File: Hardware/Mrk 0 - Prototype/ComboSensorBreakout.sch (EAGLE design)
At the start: 13 parts, among them J1 CONN_42.54_SCREW, Q1 DMG3404, U1 SPG30, U2 SHTC3DFN, U3 TPS7A0518DBV, U4 TXS0102DCU

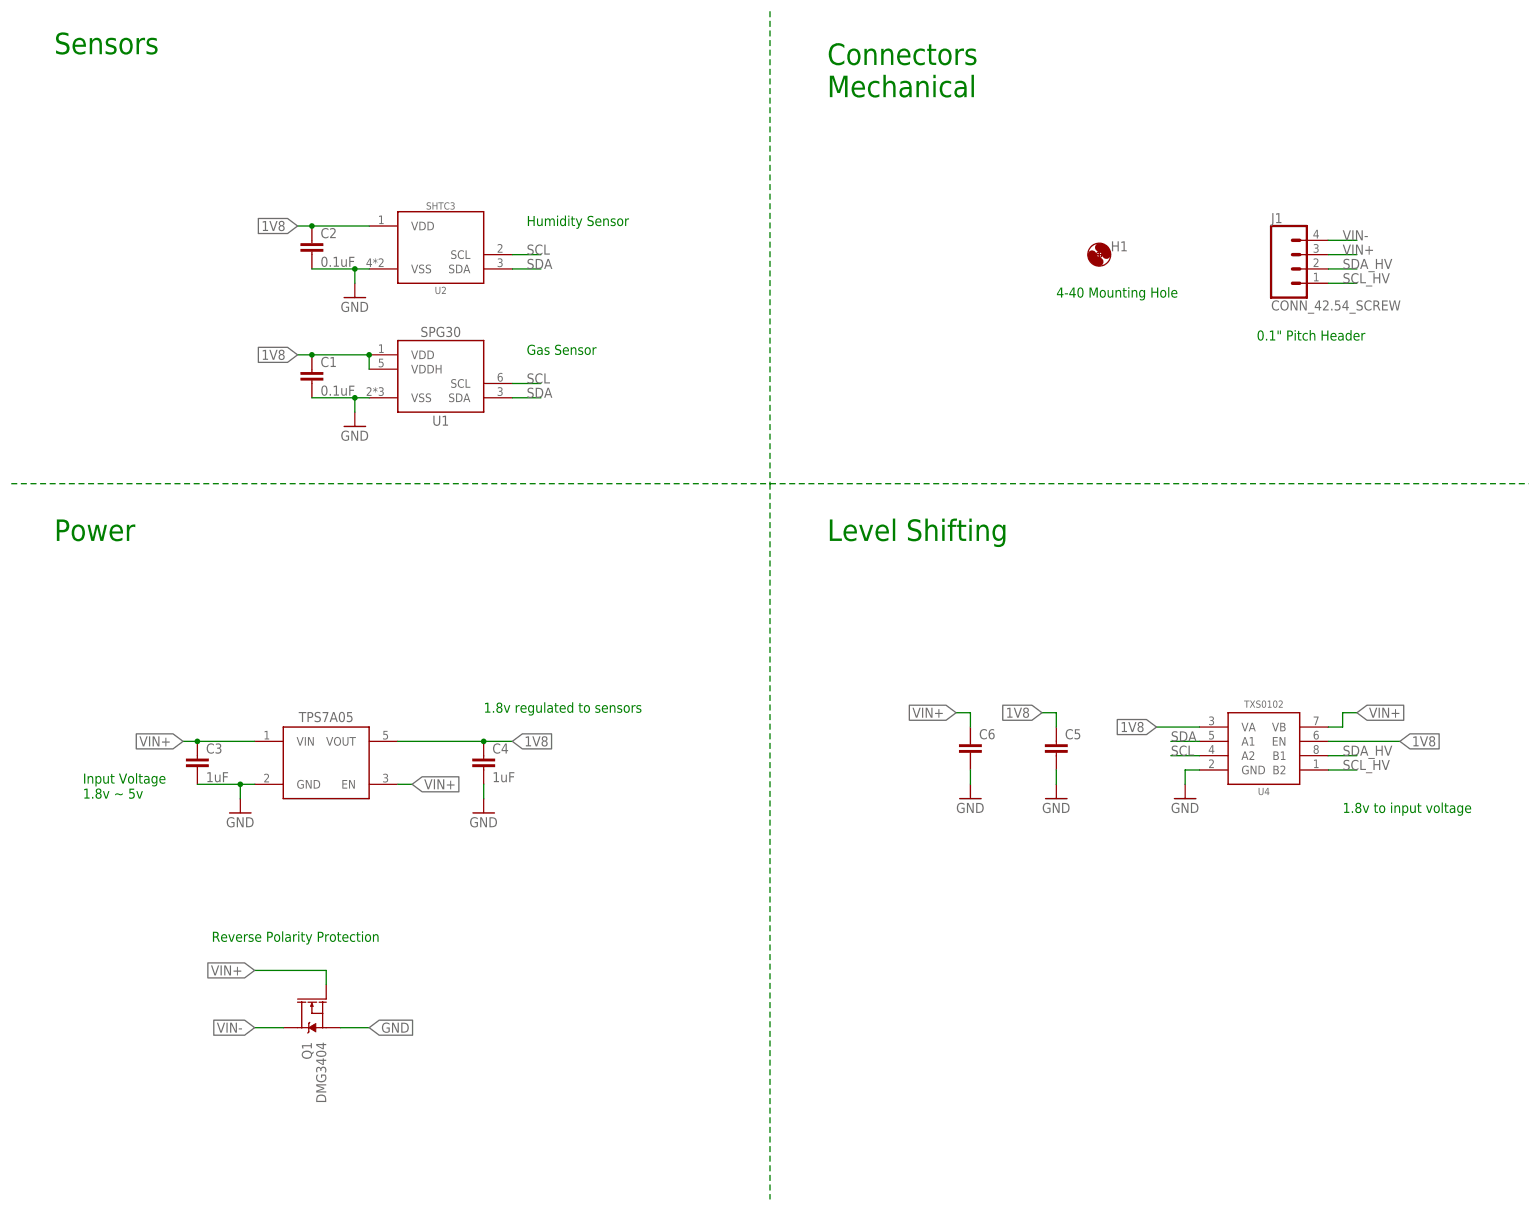
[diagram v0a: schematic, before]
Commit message: Updated/generated BoMs if not present
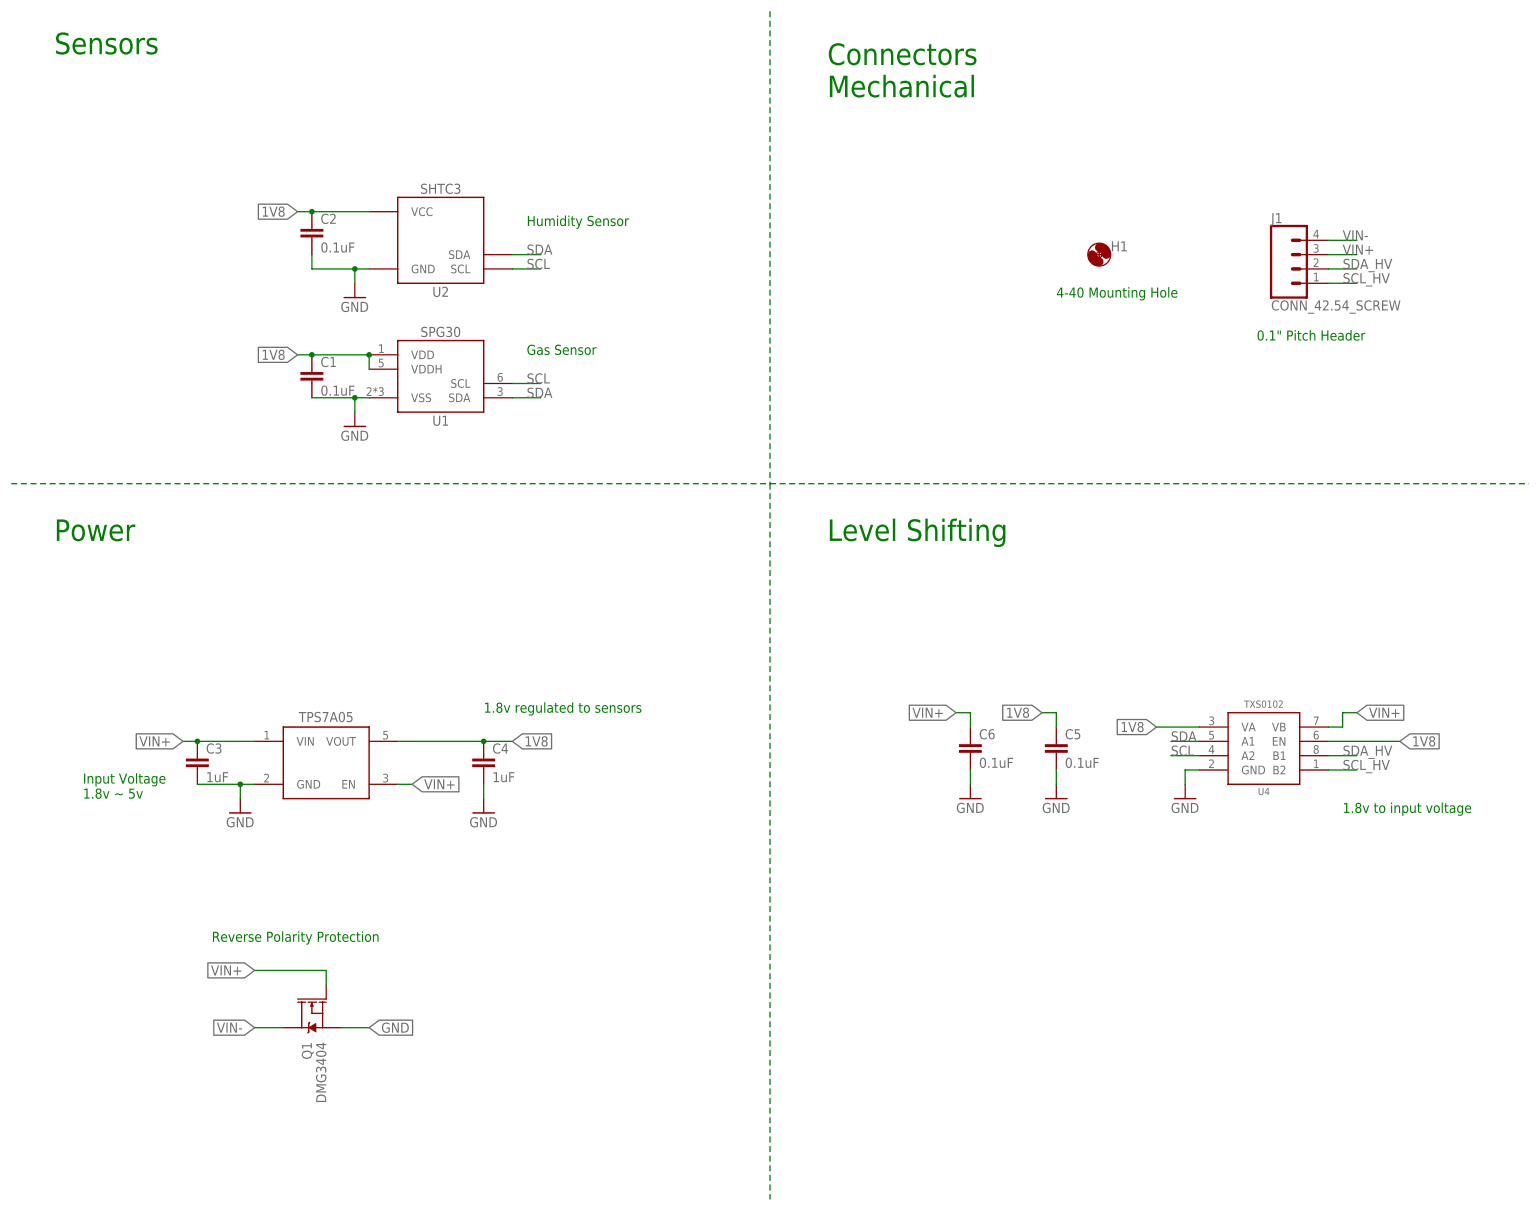
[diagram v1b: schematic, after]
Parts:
- C5, C6: value (none) -> 0.1uF
- H1: DIGIKEY (none) -> DNP; MF (none) -> N/A; MPN (none) -> DNP
- U3: DIGIKEY (none) -> 296-50251-1-ND
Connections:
- net 1V8: now also U2.VCC; no longer U2.VDD
- net GND: now also U2.GND; no longer U2.VSS
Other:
- moved on the sheet: C2
